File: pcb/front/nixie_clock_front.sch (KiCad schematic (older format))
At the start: 18 parts, among them J1 Conn_01x10_Male, J2 Conn_01x10_Male, U1 74141, U2 74141, U3 74141, U4 74141

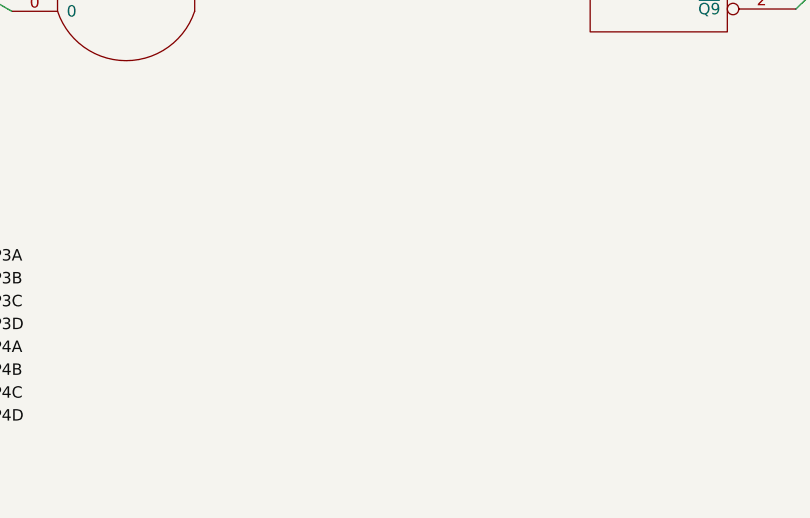
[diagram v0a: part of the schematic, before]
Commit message: Back panel PCB
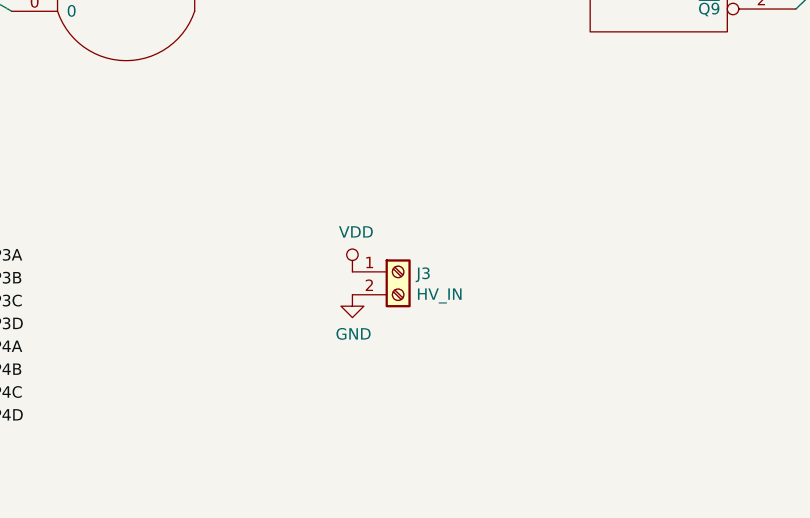
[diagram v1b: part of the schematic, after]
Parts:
- added J3: HV_IN, nixie_clock:Terminal_Block_KF301-5.0-2P, symbol Connector:Screw_Terminal_01x02
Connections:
- net GND: now also J3.2 (Pin_2)
- net VDD: now also J3.1 (Pin_1)
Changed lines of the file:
@@
+	1    0    0    -1
+$EndComp
+$Comp
+L Connector:Screw_Terminal_01x02 J3
+U 1 1 5DB25536
+P 5680 6320
+F 0 "J3" H 5760 6312 50  0000 L CNN
+F 1 "HV_IN" H 5760 6221 50  0000 L CNN
+F 2 "nixie_clock:Terminal_Block_KF301-5.0-2P" H 5680 6320 50  0001 C CNN
+F 3 "~" H 5680 6320 50  0001 C CNN
+	1    5680 6320
+	1    0    0    -1
+$EndComp
+$Comp
+L power:GND #PWR0117
+U 1 1 5DB25DE2
+P 5480 6420
+F 0 "#PWR0117" H 5480 6170 50  0001 C CNN
+F 1 "GND" H 5485 6247 50  0000 C CNN
+F 2 "" H 5480 6420 50  0001 C CNN
+F 3 "" H 5480 6420 50  0001 C CNN
+	1    5480 6420
+	1    0    0    -1
+$EndComp
+$Comp
+L power:VDD #PWR0118
+U 1 1 5DB267B5
+P 5480 6320
+F 0 "#PWR0118" H 5480 6170 50  0001 C CNN
+F 1 "VDD" H 5497 6493 50  0000 C CNN
+F 2 "" H 5480 6320 50  0001 C CNN
+F 3 "" H 5480 6320 50  0001 C CNN
+	1    5480 6320
 	1    0    0    -1
 $EndComp
